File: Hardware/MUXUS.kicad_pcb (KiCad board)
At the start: 4 copper layers, 99.1 x 99.1 mm, 124 parts, among them J1 USB_C_Receptacle_USB2.0, J10 VCP, J2 USB_B, J3 USB_A, J4 USB_B, J5 USB_A, J6 STDC14, J7 USB_B, J8 USB_A, J9 SWD, SW1 USER, SW2 RESET, U1 USBLC6-4SC6, U10 AP2151W, U11 AOZ1212AI, U12 USBLC6-2SC6, U13 USBLC6-2SC6, U14 AP2151W, U2 USB2504A-JT, U3 USBLC6-2SC6, U4 USBLC6-2SC6, U5 AP2151W, U6 TS3USBCA420RSVR, U7 STM32G431K8T6, U8 USBLC6-2SC6, U9 USBLC6-2SC6, Y1 ATS240C

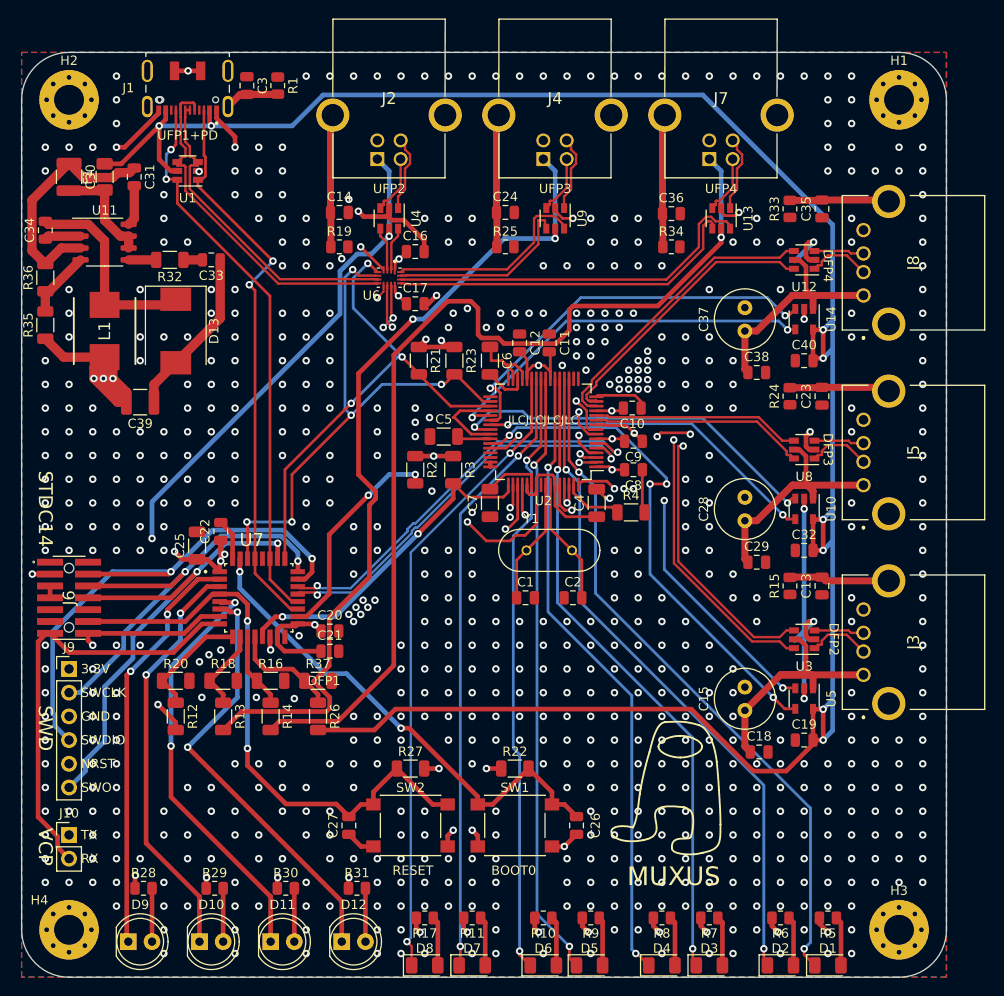
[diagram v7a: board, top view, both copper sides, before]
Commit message: Repaired routing and fixed some 3d models
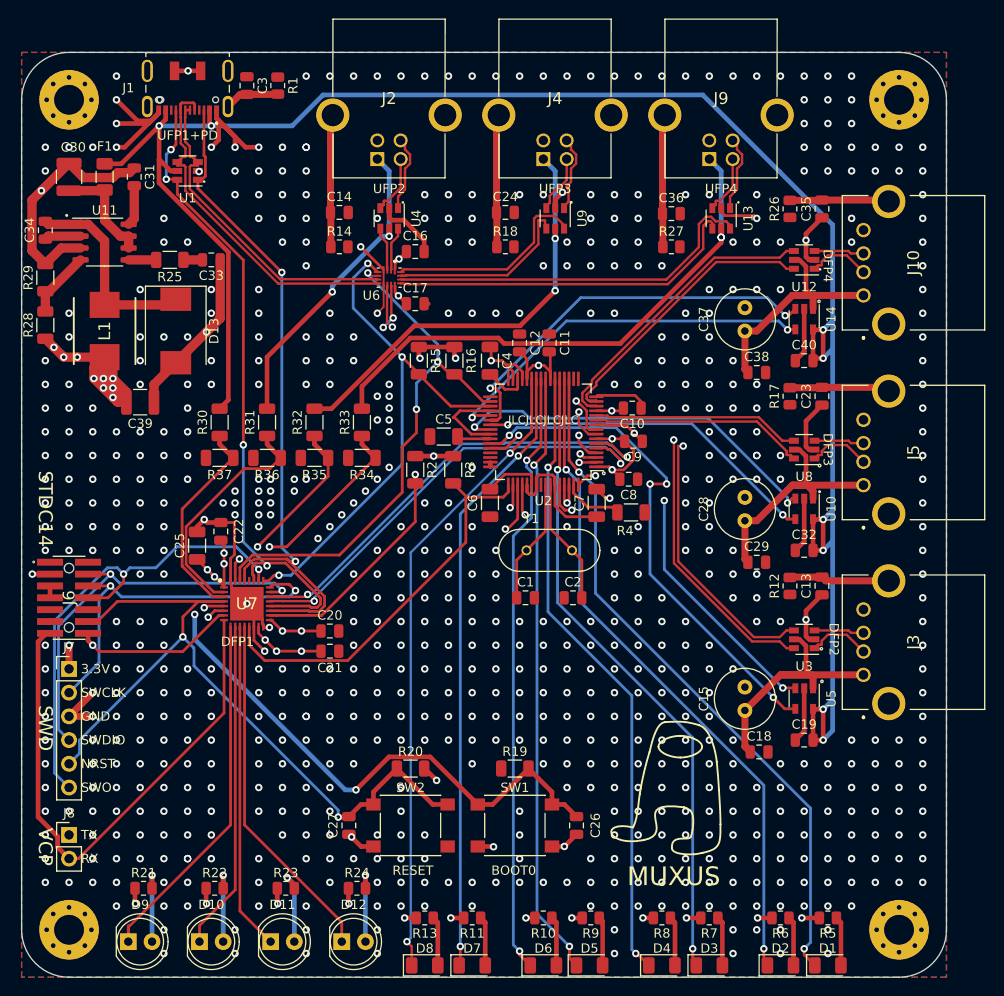
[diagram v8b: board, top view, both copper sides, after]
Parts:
- removed the R14 at (41.9, 86.4)
- removed the R16 at (41.9, 82.5)
- removed the R18 at (36.8, 82.5)
- added R32: 10K, Resistor_SMD:R_1206_3216Metric, F.Cu at (46.6, 54.9)
- added R35: 1K, Resistor_SMD:R_1206_3216Metric, F.Cu at (46.6, 58.7)
- added R36: 1K, Resistor_SMD:R_1206_3216Metric, F.Cu at (41.5, 58.7)
- U7: value STM32G431K8T6 -> STM32G441KBU6; footprint STM32G431K8T6:STM32G431K8T6 -> STM32G441KBU6:STM32G441KBU6
- moved R30 31.8 mm to (36.4, 54.9), turned to 90 degrees
- moved R31 31.8 mm to (41.5, 54.9), turned to 90 degrees
- moved R33 31.8 mm to (51.7, 54.9), turned to 90 degrees
- moved R34 24.3 mm to (51.7, 58.7), turned to 180 degrees
- moved R37 24.3 mm to (36.4, 58.7), turned to 180 degrees
- moved U7 1.42 mm to (39.4, 74.3)
- moved C8 1.14 mm to (80.3, 61.0)
- renumbered C6 to C4, C7 to C6, C4 to C7, J8 to J10, J9 to J7, J10 to J8, J7 to J9, R15 to R12, R17 to R13, R19 to R14, R21 to R15, R23 to R16, R24 to R17, R25 to R18, R22 to R19, R27 to R20, R28 to R21, R29 to R22, R30 to R23, R31 to R24, R32 to R25, R33 to R26, R34 to R27, R35 to R28, R36 to R29, R12 to R30, R13 to R31, R26 to R33, R37 to R34, R20 to R37
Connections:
- D10 pad 1: UI_LED2 -> LED2
- D11 pad 1: UI_LED3 -> LED3
- D12 pad 1: UI_LED4 -> LED4
- D9 pad 1: UI_LED1 -> LED1
- R30 pad 1: Net-(R12-Pad1) -> VOLT1
- R30 pad 2: UFP2_VBUS -> UFP1_VBUS
- R31 pad 1: Net-(R13-Pad1) -> VOLT2
- R31 pad 2: UFP3_VBUS -> UFP2_VBUS
- R33 pad 1: Net-(R26-Pad1) -> VOLT4
- R33 pad 2: UFP1_VBUS -> UFP4_VBUS
- R34 pad 1: Net-(R26-Pad1) -> VOLT4
- R37 pad 1: Net-(R12-Pad1) -> VOLT1
- U7 pad 10: Net-(R13-Pad1) -> LED2
- U7 pad 11: Net-(R14-Pad1) -> LED3
- U7 pad 12: Net-(R26-Pad1) -> LED4
- U7 pad 2: UI_LED1 -> VOLT2
- U7 pad 3: UI_LED2 -> VOLT1
- U7 pad 5: UI_LED3 -> VOLT3
- U7 pad 6: UI_LED4 -> VOLT4
- U7 pad 9: Net-(R12-Pad1) -> LED1
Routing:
- net UFP4_VBUS: track 106.5 -> 58.1 mm, vias 1 -> 2
- net UI_LED4: track 46.4 -> 0.00 mm, vias 2 -> 0
- net UI_LED3: track 45.3 -> 0.00 mm, vias 2 -> 0
- net UI_LED2: track 44.5 -> 0.00 mm, vias 2 -> 0
- net UI_LED1: track 44.4 -> 0.00 mm, vias 2 -> 0
- net UFP3_VBUS: track 89.6 -> 46.7 mm
- net UFP2_VBUS: track 75.0 -> 33.9 mm, vias 3 -> 2
- net LED1: track 0.00 -> 40.2 mm
- net LED4: track 0.00 -> 38.1 mm
- net LED2: track 0.00 -> 35.3 mm
- net LED3: track 0.00 -> 35.1 mm
- net VOLT4: track 0.00 -> 30.5 mm, vias 0 -> 2
- net UFP1_VBUS: track 244.1 -> 216.3 mm
- net VOLT3: track 0.00 -> 26.7 mm, vias 0 -> 2
- net VOLT2: track 0.00 -> 25.5 mm
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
